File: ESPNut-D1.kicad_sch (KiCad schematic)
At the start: 48 parts

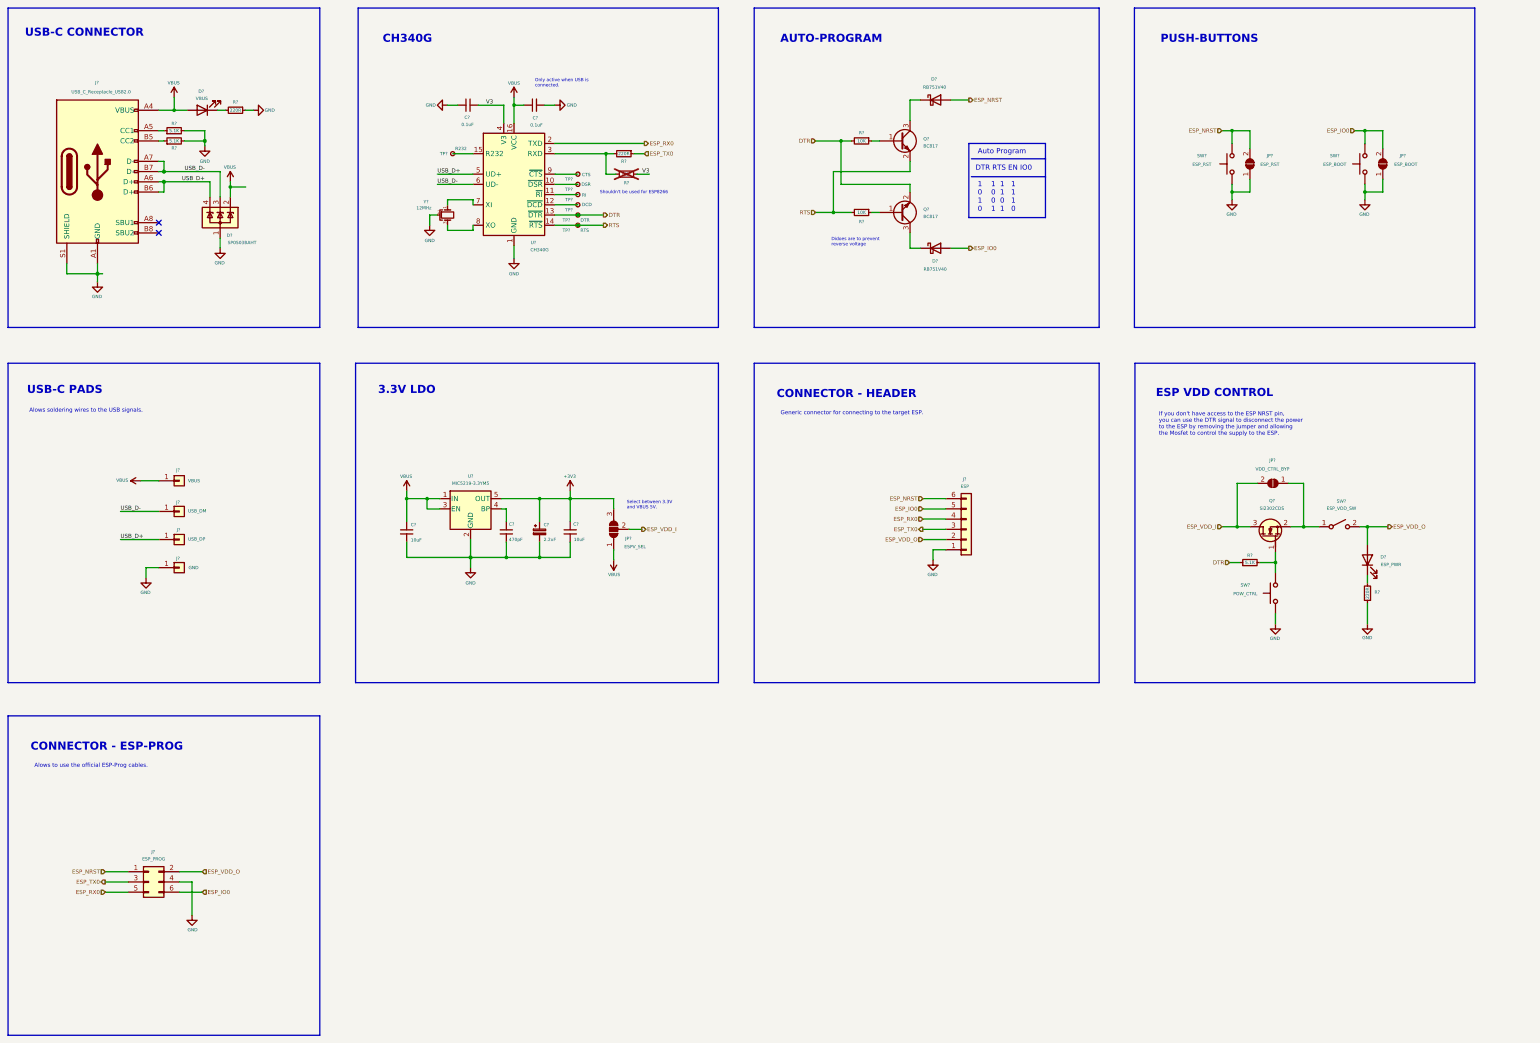
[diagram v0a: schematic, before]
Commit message: Updated project version to KiCad V9
- Updated text colors.
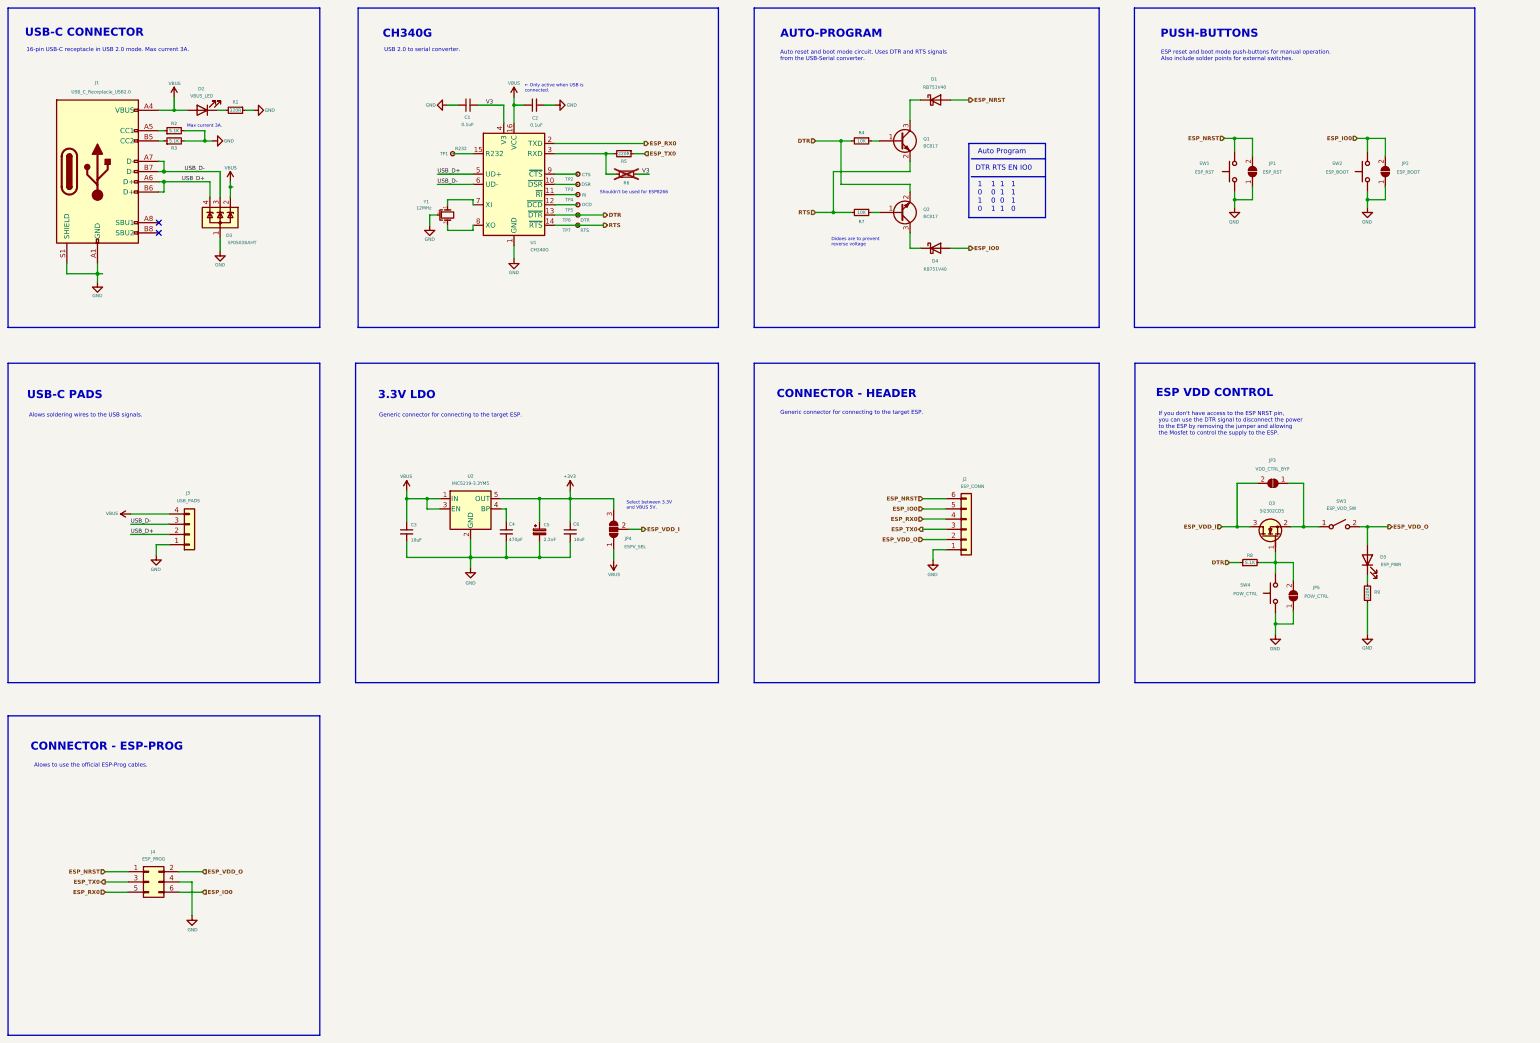
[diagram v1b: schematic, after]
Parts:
- removed J?: VBUS, symbol Connector_Generic:Conn_01x01
- removed J?: USB_DM, symbol Connector_Generic:Conn_01x01
- removed J?: GND, symbol Connector_Generic:Conn_01x01
- removed J?: USB_DP, symbol Connector_Generic:Conn_01x01
- added J3: USB_PADS, CIRCUITSTATE_Solderpads:Solderpad_1x4_Rectangular_Rounded_1.2x1mm_P1.5mm, symbol Connector_Generic:Conn_01x04
- added JP5: POW_CTRL, CIRCUITSTATE_Solder-Jumper:SolderJumper-2_P1.3mm_Open_RoundedPad1.0x1.2mm, symbol Jumper:SolderJumper_2_Open
- C1, C2, C3, C4, C6: renamed from C?; footprint Capacitor_SMD:C_0603_1608Metric_Pad1.08x0.95mm_HandSolder -> Capacitor_SMD:C_0402_1005Metric
- D2: renamed from D?; value VBUS -> VBUS_LED; footprint LED_SMD:LED_0805_2012Metric_Pad1.15x1.40mm_HandSolder -> LED_SMD:LED_0603_1608Metric; Name (none) -> VBUS_LED
- D3: renamed from D?; MFR (none) -> Littelfuse; Mfr Littelfuse -> (none)
- D5: renamed from D?; footprint LED_SMD:LED_0805_2012Metric_Pad1.15x1.40mm_HandSolder -> LED_SMD:LED_0603_1608Metric; Name (none) -> ESP_PWR
- J1: renamed from J?; MFR (none) -> Korean Hroparts Elec; Mfr Korean Hroparts Elec -> (none); Name (none) -> USB-C
- J2: renamed from J?; value ESP -> ESP_CONN; footprint (none) -> Connector_PinHeader_2.54mm:PinHeader_1x06_P2.54mm_Vertical; Name (none) -> ESP_CONN
- J4: renamed from J?; footprint (none) -> Connector_PinHeader_1.27mm:PinHeader_2x03_P1.27mm_Vertical; Name (none) -> ESP_PROG
- JP1: renamed from JP?; footprint CIRCUITSTATE_Jumper_SMD:SolderJumper-2_P1.3mm_Open_Rounded-Pad_0.85x1mm -> CIRCUITSTATE_Solder-Jumper:SolderJumper-2_P1.3mm_Open_RoundedPad1.0x1.2mm; Name (none) -> ESP_RST
- JP2: renamed from JP?; footprint CIRCUITSTATE_Jumper_SMD:SolderJumper-2_P1.3mm_Open_Rounded-Pad_0.85x1mm -> CIRCUITSTATE_Solder-Jumper:SolderJumper-2_P1.3mm_Open_RoundedPad1.0x1.2mm; Name (none) -> ESP_BOOT
- JP3: renamed from JP?; footprint CIRCUITSTATE_Jumper_SMD:SolderJumper-2_P1.3mm_Open_Rounded-Pad_0.85x1mm -> CIRCUITSTATE_Solder-Jumper:SolderJumper-2_P1.3mm_Open_RoundedPad1.0x1.2mm; Name (none) -> VDD_CTRL_BYP
- JP4: renamed from JP?; footprint (none) -> CIRCUITSTATE_Solder-Jumper:SolderJumper-3_P1.3mm_Open_RoundedPad1.0x1.5mm_NumberLabels; Name (none) -> ESPV_SEL
- R1, R4, R5, R6, R7, R9: renamed from R?; footprint Resistor_SMD:R_0603_1608Metric_Pad0.98x0.95mm_HandSolder -> Resistor_SMD:R_0402_1005Metric
- R2, R3, R8: renamed from R?; footprint Resistor_SMD:R_0402_1005Metric_Pad0.72x0.64mm_HandSolder -> Resistor_SMD:R_0402_1005Metric; MFR (none) -> Walsin; Mfr Walsin -> (none)
- SW1: renamed from SW?; Name (none) -> ESP_RST
- SW2: renamed from SW?; Name (none) -> ESP_BOOT
- SW3: renamed from SW?; footprint (none) -> Button_Switch_SMD:SW_SPDT_PCM12; Name (none) -> ESP_VDD_SW
- SW4: renamed from SW?; Name (none) -> POW_CTRL
- TP1: renamed from TP?; footprint (none) -> CIRCUITSTATE_Solderpads:Solder-Pad_Rectangular_W0.6mm; Name (none) -> R232
- TP2: renamed from TP?; footprint (none) -> CIRCUITSTATE_Solderpads:Solder-Pad_Rectangular_W0.6mm; Name (none) -> CTS
- TP3: renamed from TP?; footprint (none) -> CIRCUITSTATE_Solderpads:Solder-Pad_Rectangular_W0.6mm; Name (none) -> DSR
- TP4: renamed from TP?; footprint (none) -> CIRCUITSTATE_Solderpads:Solder-Pad_Rectangular_W0.6mm; Name (none) -> RI
- TP5: renamed from TP?; footprint (none) -> CIRCUITSTATE_Solderpads:Solder-Pad_Rectangular_W0.6mm; Name (none) -> DCD
- TP6: renamed from TP?; footprint (none) -> CIRCUITSTATE_Solderpads:Solder-Pad_Rectangular_W0.6mm; Name (none) -> DTR
- TP7: renamed from TP?; footprint (none) -> CIRCUITSTATE_Solderpads:Solder-Pad_Rectangular_W0.6mm; Name (none) -> RTS
- U2: renamed from U?; Name (none) -> 3.3V
- gave numbers to parts that had none: 8
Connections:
- net GND: now also J3.1 (Pin_1), JP5.1 (A)
- net USB_D+: now also J3.2 (Pin_2)
- net USB_D-: now also J3.3 (Pin_3)
- net VBUS: now also J3.4 (Pin_4)
- net at Q3.1 (G), R8.2, SW4.2: now also JP5.2 (B)
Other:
- note added: "Max current 3A."
- note added: "← Only active when USB is connected."
- note removed: "Only active when USB is connected."
- moved on the sheet: JP1, JP2, SW1, SW2

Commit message: Placement completed
- Added breakout pads for the LEDs.
- Changed USB-C connector footprint to SMD one.
- Added PCB outline.
- Placed all components.
- Added silkscreen labels and logos.
- Routing pending.
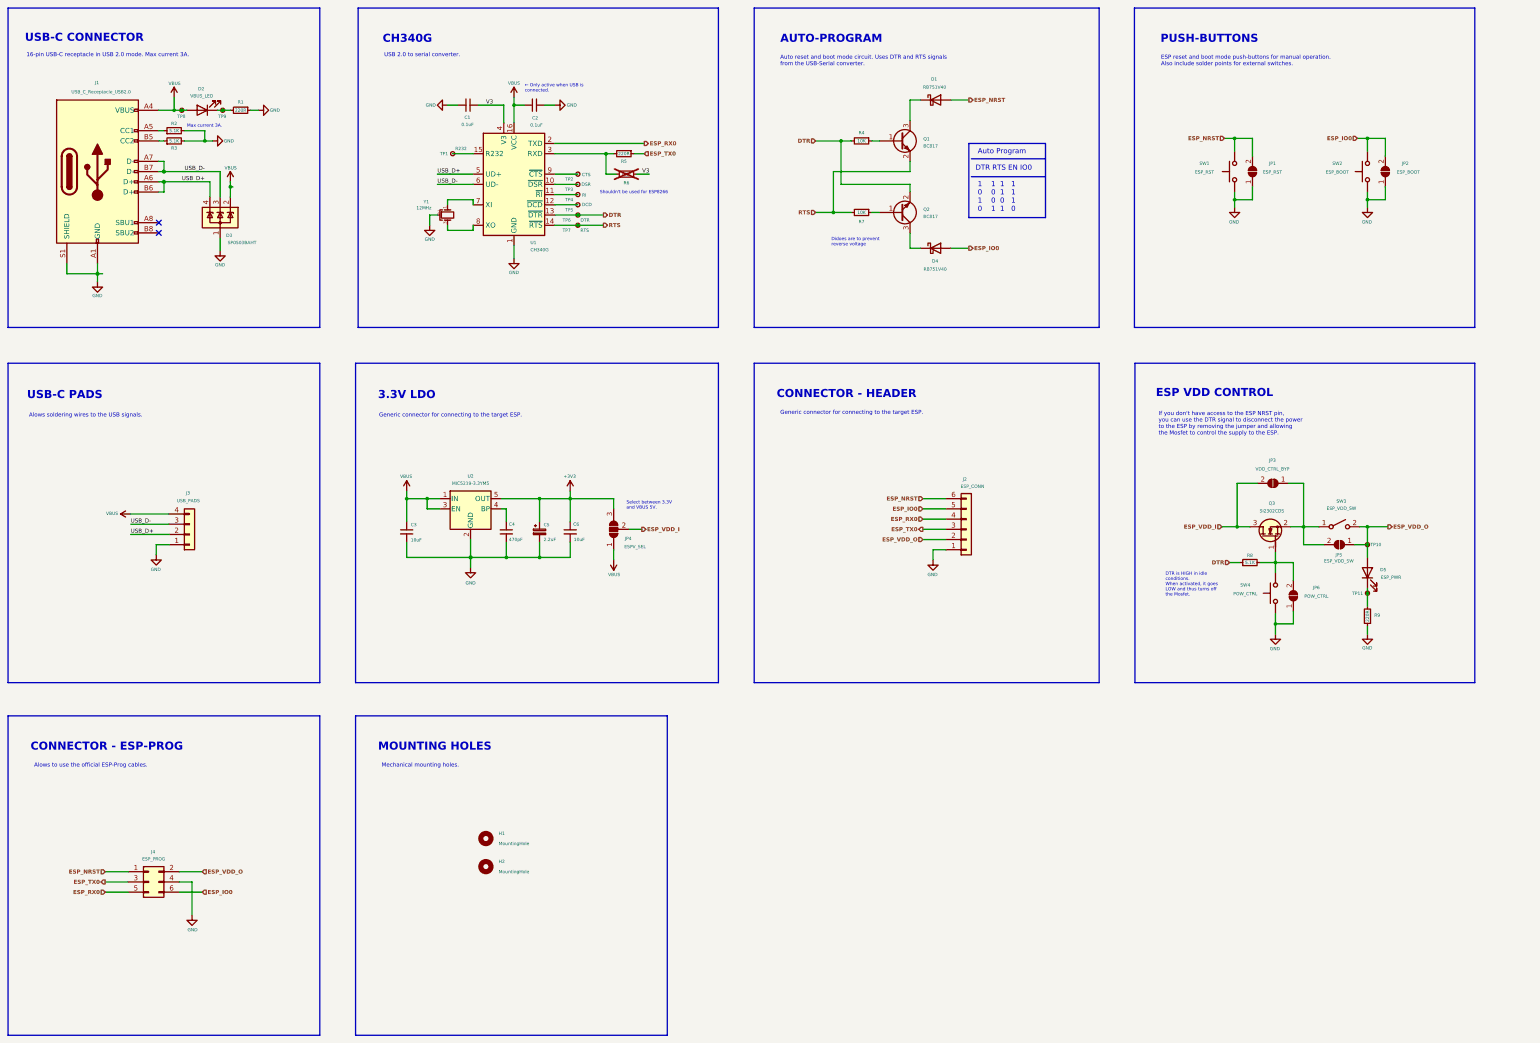
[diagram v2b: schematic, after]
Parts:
- added H1, H2: MountingHole, MountingHole:MountingHole_2.2mm_M2_DIN965, symbol Mechanical:MountingHole
- added JP5: ESP_VDD_SW, CSE_Solder-Jumper:Solder-Jumper-1x2_P1.3mm_Open_Rounded_1.0x1.2mm, symbol Jumper:SolderJumper_2_Open
- added TP10, TP11, TP8, TP9: CTS, SparkFun-Connector:TestPoint-0.75mm, symbol Connector:TestPoint_Small
- J1: footprint CIRCUITSTATE_Connector_USB:Korean-Hroparts-Elec_TYPE-C-31-M-12 -> CSE_Connector_USB:USB_C_Receptacle_GCT_USB4110
- J3: footprint CIRCUITSTATE_Solderpads:Solderpad_1x4_Rectangular_Rounded_1.2x1mm_P1.5mm -> CSE_Solderpads:Solderpad_1x4_Rectangular_Rounded_1.2x1mm_P1.5mm
- JP1, JP2, JP3: footprint CIRCUITSTATE_Solder-Jumper:SolderJumper-2_P1.3mm_Open_RoundedPad1.0x1.2mm -> CSE_Solder-Jumper:Solder-Jumper-1x2_P1.3mm_Open_Rounded_1.0x1.2mm
- JP4: footprint CIRCUITSTATE_Solder-Jumper:SolderJumper-3_P1.3mm_Open_RoundedPad1.0x1.5mm_NumberLabels -> CSE_Solder-Jumper:Solder-Jumper-1x3_P1.3mm_Open_Rounded_1.0x1.5mm_Labels
- JP6: renamed from JP5; footprint CIRCUITSTATE_Solder-Jumper:SolderJumper-2_P1.3mm_Open_RoundedPad1.0x1.2mm -> CSE_Solder-Jumper:Solder-Jumper-1x2_P1.3mm_Open_Rounded_1.0x1.2mm
- SW1, SW2, SW4: footprint CIRCUITSTATE_Switch_SMD:CK_SW_SPST_UK-B0273-SP25Y -> CSE_Switch_SMD:CK_SW_SPST_UK-B0273-SP25Y
- TP1, TP2, TP3, TP4, TP5, TP6, TP7: footprint CIRCUITSTATE_Solderpads:Solder-Pad_Rectangular_W0.6mm -> SparkFun-Connector:TestPoint-0.75mm
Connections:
- net ESP_VDD_O: now also JP5.1 (A), TP10.1
- net VBUS: now also TP8.1
- net at D5.1 (K), R9.2: now also TP11.1
- net at JP3.1 (A), Q3.2 (S), SW3.1 (A): now also JP5.2 (B)
- net at D2.1 (K), R1.2: now also TP9.1
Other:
- note added: "MOUNTING HOLES"
- moved on the sheet: D5, R1, R9

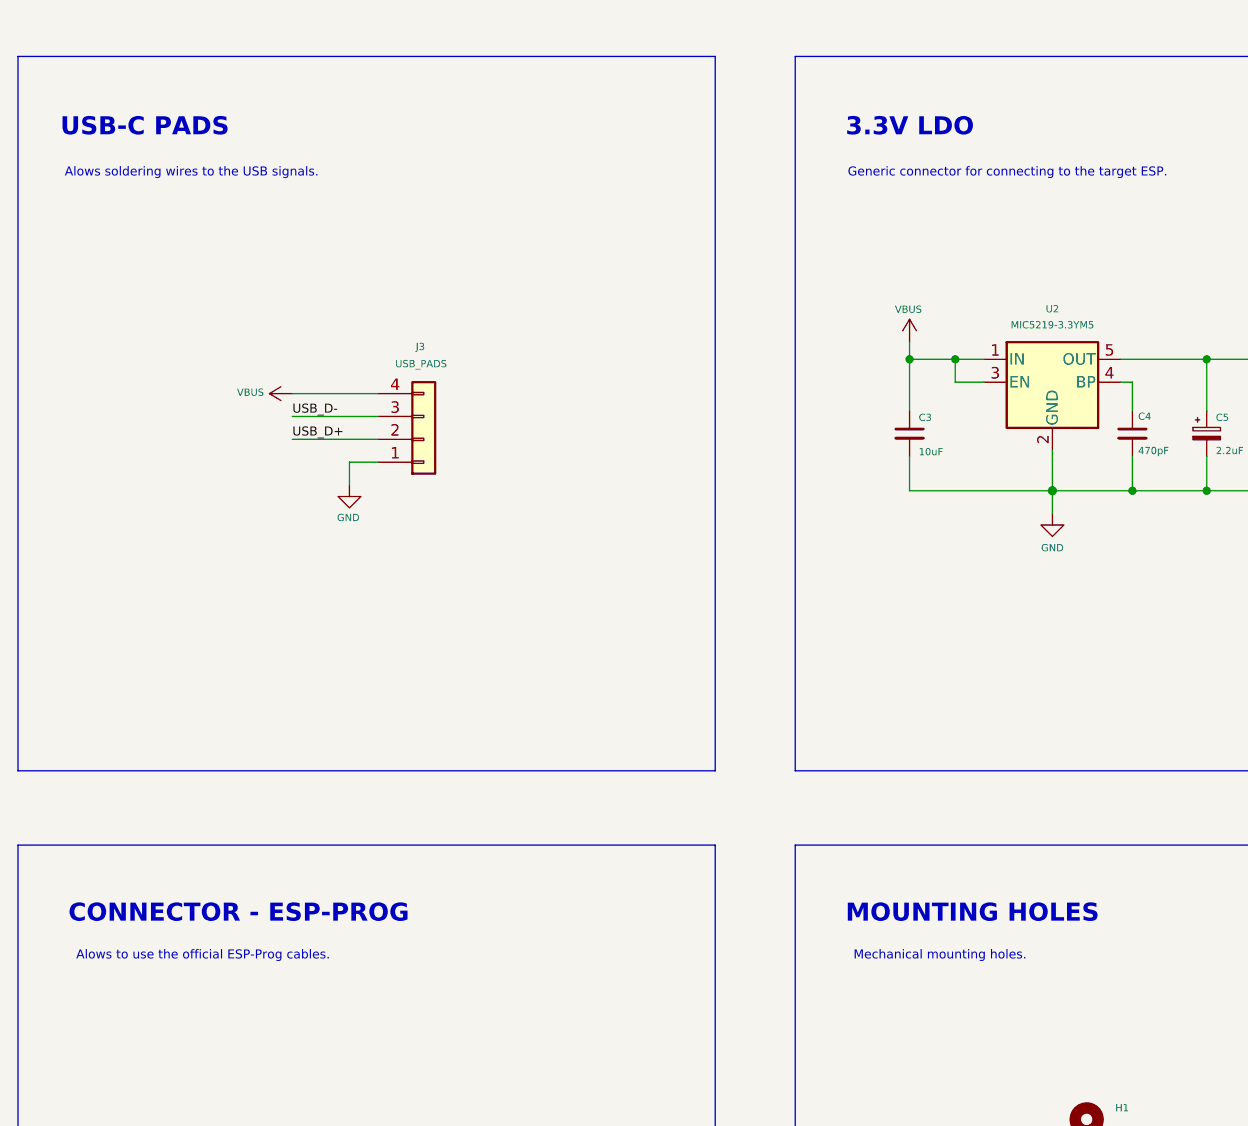
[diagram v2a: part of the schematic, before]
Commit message: Routing completed
- Added GND zones.
- DRC passes.
- Added more silkscreen labels.
- Added CIRCUITSTATE logo on the back silkscreen.
- Updated Fab layers.
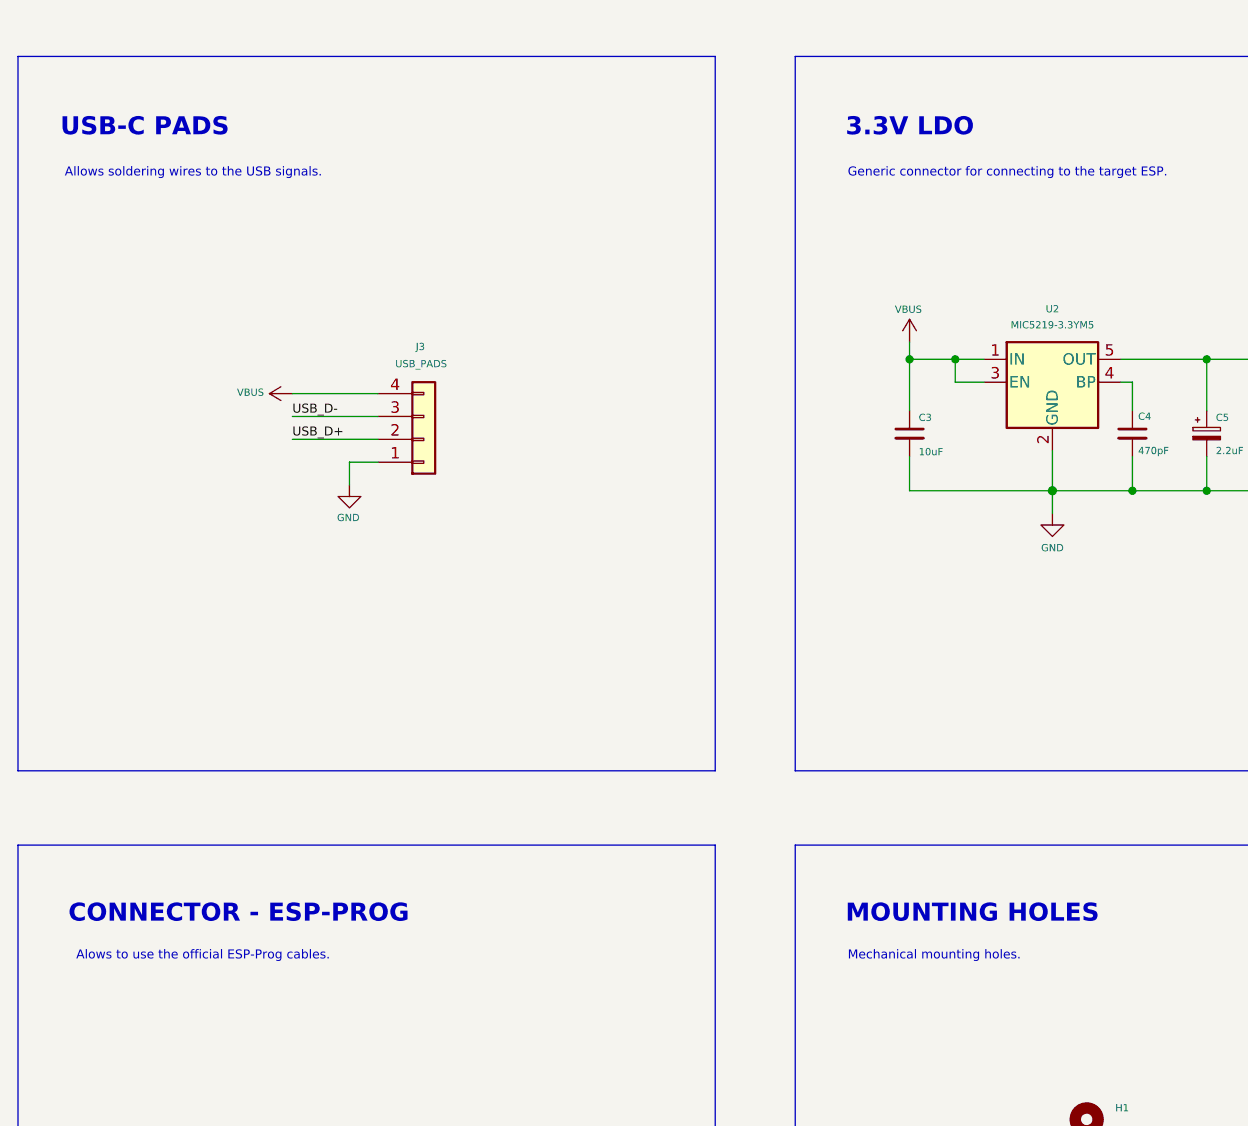
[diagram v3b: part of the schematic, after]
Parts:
- Q3: footprint Package_TO_SOT_SMD_AKL:SOT-23 -> Package_TO_SOT_SMD:SOT-23
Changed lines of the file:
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@@
 	(title_block
 		(title "ESPNut-D1")
-		(date "2025-04-05")
+		(date "2025-04-08")
 		(rev "0.1")
 		(company "CIRCUITSTATE Electronics LLP")
@@
 	(text_box "Mechanical mounting holes."
 		(exclude_from_sim no)
-		(at 114.935 207.645 0)
+		(at 114.3 207.645 0)
 		(size 39.37 2.54)
 		(margins 0.7499 0.7499 0.7499 0.7499)
@@
 		)
 	)
-	(text_box "Alows soldering wires to the USB signals."
+	(text_box "Allows soldering wires to the USB signals."
 		(exclude_from_sim no)
 		(at 27.305 120.65 0)
@@
 		(stroke
 			(width -0.0001)
-			(type default)
+			(type solid)
 		)
 		(fill
@@
 			)
 		)
-		(property "Footprint" "Package_TO_SOT_SMD_AKL:SOT-23"
+		(property "Footprint" "Package_TO_SOT_SMD:SOT-23"
 			(at 334.01 147.32 0)
 			(effects
